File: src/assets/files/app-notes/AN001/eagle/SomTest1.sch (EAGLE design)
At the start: 43 parts, among them J1 SPARK_M.2EKEY, U1 MAX17043, U2 BQ24195, U3 XCL223

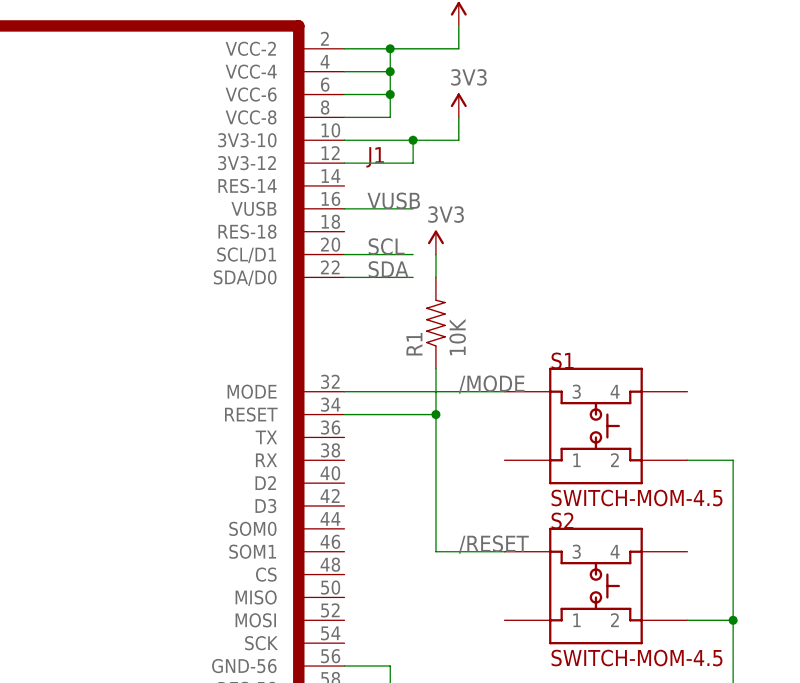
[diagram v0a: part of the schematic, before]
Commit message: Fix M.2 example
M.2 pin 40 should be D3 and M.2 pin 42 should be D2. These were reversed previously, however
this sample board does not use the pins.
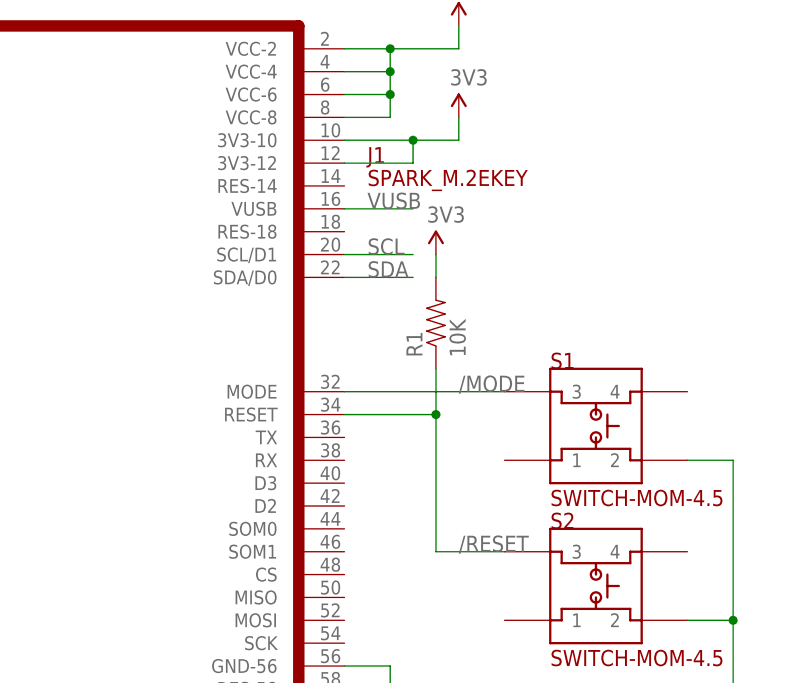
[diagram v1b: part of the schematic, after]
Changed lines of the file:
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@@
 <?xml version="1.0" encoding="utf-8"?>
 <!DOCTYPE eagle SYSTEM "eagle.dtd">
-<eagle version="9.4.0">
+<eagle version="9.6.2">
 <drawing>
 <settings>
-<setting alwaysvectorfont="yes"/>
+<setting alwaysvectorfont="no"/>
 <setting verticaltext="up"/>
 </settings>
@@
 <layer number="1" name="Top" color="4" fill="1" visible="no" active="no"/>
 <layer number="2" name="Route2" color="1" fill="3" visible="no" active="no"/>
+<layer number="3" name="Route3" color="17" fill="1" visible="no" active="no"/>
+<layer number="4" name="Route4" color="18" fill="1" visible="no" active="no"/>
+<layer number="5" name="Route5" color="19" fill="1" visible="no" active="no"/>
+<layer number="6" name="Route6" color="25" fill="1" visible="no" active="no"/>
+<layer number="7" name="Route7" color="26" fill="1" visible="no" active="no"/>
+<layer number="8" name="Route8" color="27" fill="1" visible="no" active="no"/>
+<layer number="9" name="Route9" color="28" fill="1" visible="no" active="no"/>
+<layer number="10" name="Route10" color="29" fill="1" visible="no" active="no"/>
+<layer number="11" name="Route11" color="30" fill="1" visible="no" active="no"/>
+<layer number="12" name="Route12" color="20" fill="1" visible="no" active="no"/>
+<layer number="13" name="Route13" color="21" fill="1" visible="no" active="no"/>
+<layer number="14" name="Route14" color="22" fill="1" visible="no" active="no"/>
 <layer number="15" name="Route15" color="4" fill="6" visible="no" active="no"/>
 <layer number="16" name="Bottom" color="1" fill="1" visible="no" active="no"/>
@@
 <part name="S1" library="rickk2" deviceset="SWITCH-MOM-4.5" device=""/>
 <part name="S2" library="rickk2" deviceset="SWITCH-MOM-4.5" device=""/>
-<part name="J1" library="rickk2" deviceset="SPARK_M.2EKEY" device="" value=""/>
+<part name="J1" library="rickk2" deviceset="SPARK_M.2EKEY" device="" value="SPARK_M.2EKEY"/>
 <part name="C1" library="rickk2" deviceset="CAP-0.01UF-0603" device="" value="0.01uF"/>
 <part name="C3" library="rickk2" deviceset="CAP-1UF-0603.DEV" device="" value="1uF"/>
